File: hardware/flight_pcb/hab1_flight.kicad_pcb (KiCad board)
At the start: 4 copper layers, 95.9 x 90.2 mm, 75 parts, among them J1 BATTERY 4xL91, J10 OLED SSD1306 (bench), J11 BUZZER (+ / -), J12 EXPANSION, J2 POWER SWITCH (on the box), J3 STDC14 SWD+VCP, J4 SPI FLASH module, J5 IMU GY-601N1, J6 BAROMETER BMP390, J7 GPS MAX-M10S, J8 DS18B20 probe, J9 LoRa E22-400M22S (adapter), Q1 AO3401A, Q2 AO3400A, SW1 RESET, U1 STM32G474RET6, U2 MIC5219-3.3

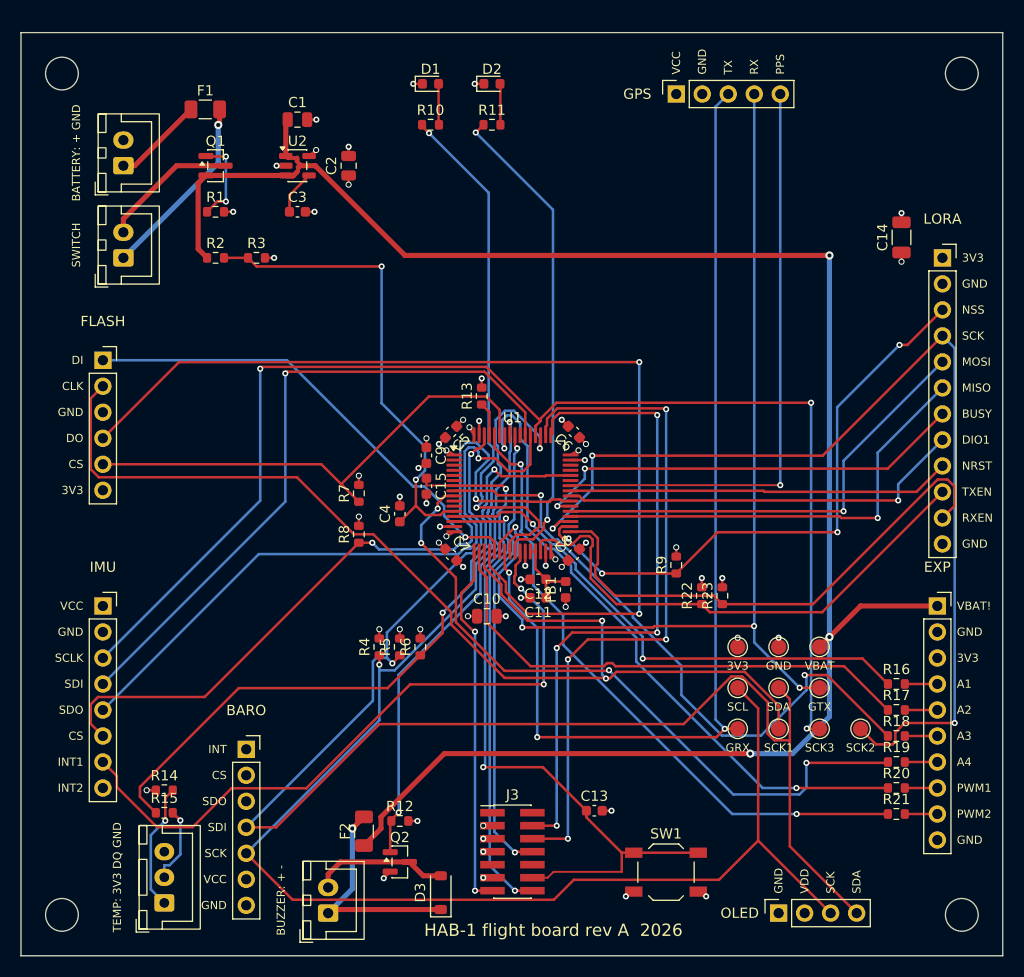
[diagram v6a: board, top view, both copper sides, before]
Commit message: flight PCB: regulator MIC5219 (SOT-23-5) -> LDL1117S33R (SOT-223), enough for LoRa TX current (HW-153)
ERC 0/0, netlist 0 mismatches, DRC 0 unconnected, 0 parity issues.
Pin order taken as the LD1117 symbol; to be confirmed against the datasheet before ordering.

Co-Authored-By: Claude Opus 5.5 (1M context) <noreply@anthropic.com>
Claude-Session: https://claude.ai/code/session_01Y9WTd2yaDzj6r4py6E8uJo
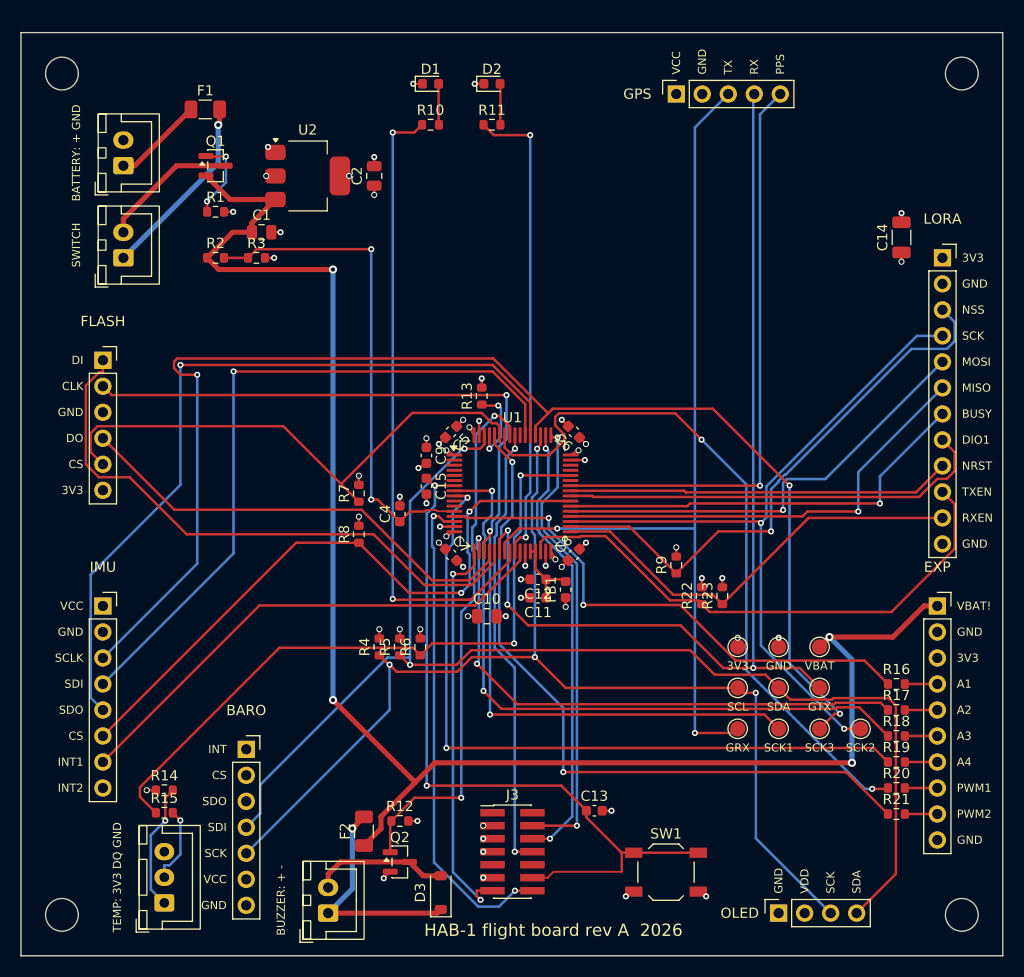
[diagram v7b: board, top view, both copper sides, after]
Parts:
- removed C3: 470p, Capacitor_SMD:C_0603_1608Metric
- C1: value 10u -> 10u 16V
- U2: value MIC5219-3.3 -> LDL1117S33R; footprint Package_TO_SOT_SMD:SOT-23-5 -> Package_TO_SOT_SMD:SOT-223-3_TabPin2
- moved C1 11.5 mm to (123.5, 119.5)
- moved C2 2.69 mm to (134.5, 114.0)
- moved U2 1.41 mm to (128.0, 114.0)
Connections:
- U2 pad 1: /VBAT_PROT -> GND
- U2 pad 2: GND -> +3V3
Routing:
- net /SPI1_MISO: track 98.6 -> 45.2 mm, vias 2 -> 0
- net /I2C_SCL: track 143.8 -> 110.4 mm, vias 2 -> 4
- net /SPI2_SCK: track 99.3 -> 70.8 mm, vias 3 -> 2
- net /VBAT_PROT: track 189.2 -> 161.6 mm, vias 3 -> 4
- net /SWCLK: track 67.6 -> 44.0 mm, vias 4 -> 2
- net /SWDIO: track 63.6 -> 45.1 mm, vias 4 -> 2
- net /IMU_INT1: track 66.6 -> 49.8 mm, vias 2 -> 0
- net /I2C_SDA: track 140.6 -> 124.6 mm
- net /USART1_RX: track 102.3 -> 88.1 mm, vias 3 -> 2
- net /SPI3_MISO: track 63.6 -> 76.7 mm
- net /IMU_CS: track 75.3 -> 63.6 mm
- net /SPI1_MOSI: track 47.1 -> 57.8 mm, vias 1 -> 0
- net /LED_ALIVE: track 52.7 -> 62.7 mm
- net /LORA_RXEN: track 51.9 -> 42.8 mm
- net /SPI1_SCK: track 110.5 -> 102.6 mm, vias 2 -> 3
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
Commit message: flight PCB: LDL1117 pinout confirmed from the datasheet; LoRa bulk capacitor 47u -> 4.7u to stay inside its stability chart (HW-153)
DS12022 rev 7: pins 1 GND, 2 VOUT, 3 VIN, tab VOUT; theta-JA 120 C/W; stability chart up to 22 uF.
ERC 0/0, netlist 0 mismatches, DRC 0 unconnected, 0 parity issues.

Co-Authored-By: Claude Opus 5.5 (1M context) <noreply@anthropic.com>
Claude-Session: https://claude.ai/code/session_01Y9WTd2yaDzj6r4py6E8uJo
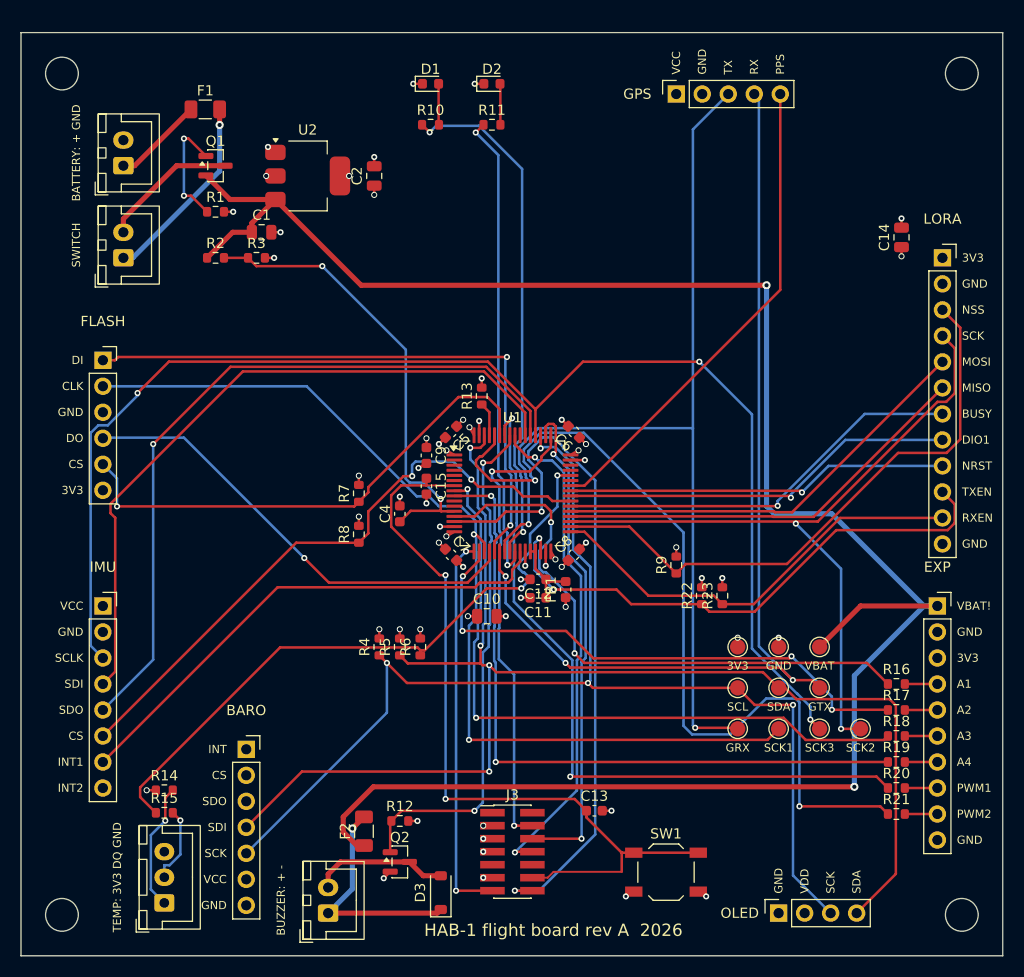
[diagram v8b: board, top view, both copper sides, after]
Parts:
- C14: value 47u -> 4.7u; footprint Capacitor_SMD:C_1206_3216Metric -> Capacitor_SMD:C_0805_2012Metric
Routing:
- net /VBAT_PROT: track 161.6 -> 199.9 mm, vias 4 -> 2
- net /VCP_TX: track 48.2 -> 70.7 mm
- net /EXP_PWM2: track 70.1 -> 85.3 mm
- net /LED_ALIVE: track 62.7 -> 50.8 mm
- net /GPS_PPS: track 57.6 -> 47.5 mm, vias 1 -> 0
- net /USART1_RX: track 88.1 -> 97.3 mm
- net /I2C_SDA: track 124.6 -> 133.0 mm, vias 2 -> 4
- net /SPI1_SCK: track 102.6 -> 96.6 mm, vias 3 -> 2
- net /EXP_A1: track 52.1 -> 57.9 mm
- net /I2C_SCL: track 110.4 -> 115.9 mm
- net /SWO: track 44.0 -> 49.0 mm
- net /SWCLK: track 44.0 -> 48.7 mm
- net /SPI3_MISO: track 76.7 -> 72.1 mm
- net /BOOT0: track 7.76 -> 3.31 mm, vias 2 -> 0
- net /NRST: track 73.2 -> 77.5 mm
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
